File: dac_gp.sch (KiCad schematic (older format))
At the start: 7 parts, among them U10 TMUX6136PWR, U11 TMUX6136PWR, U5 DAC80508ZRTER

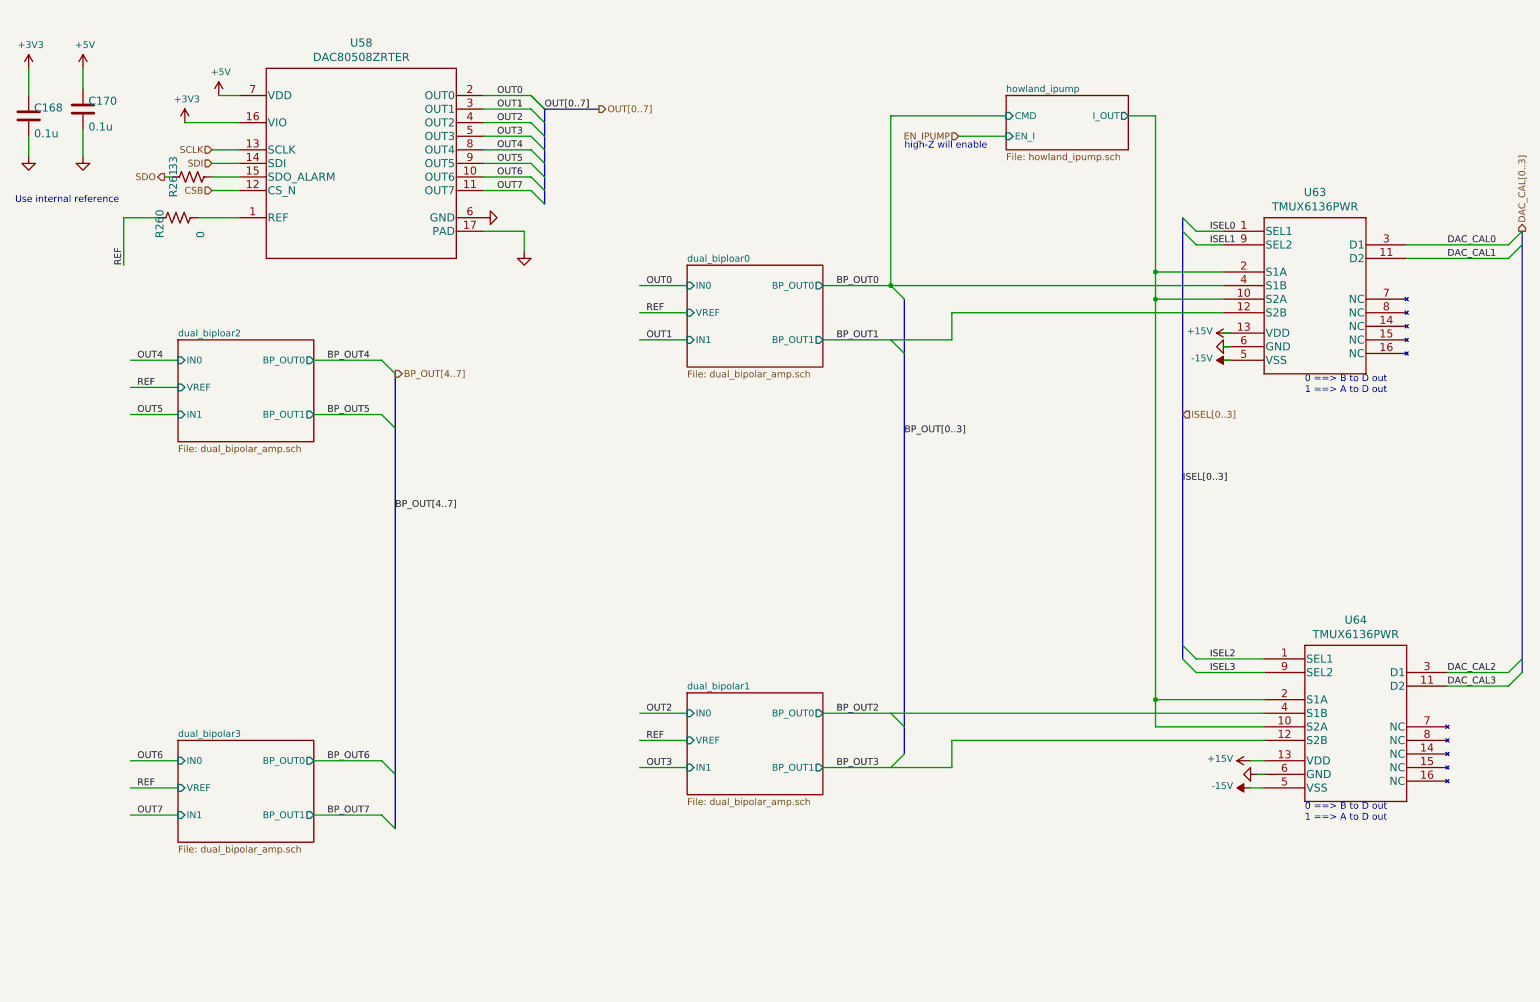
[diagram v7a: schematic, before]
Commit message: reduce ADC and DAC connections to ease routing
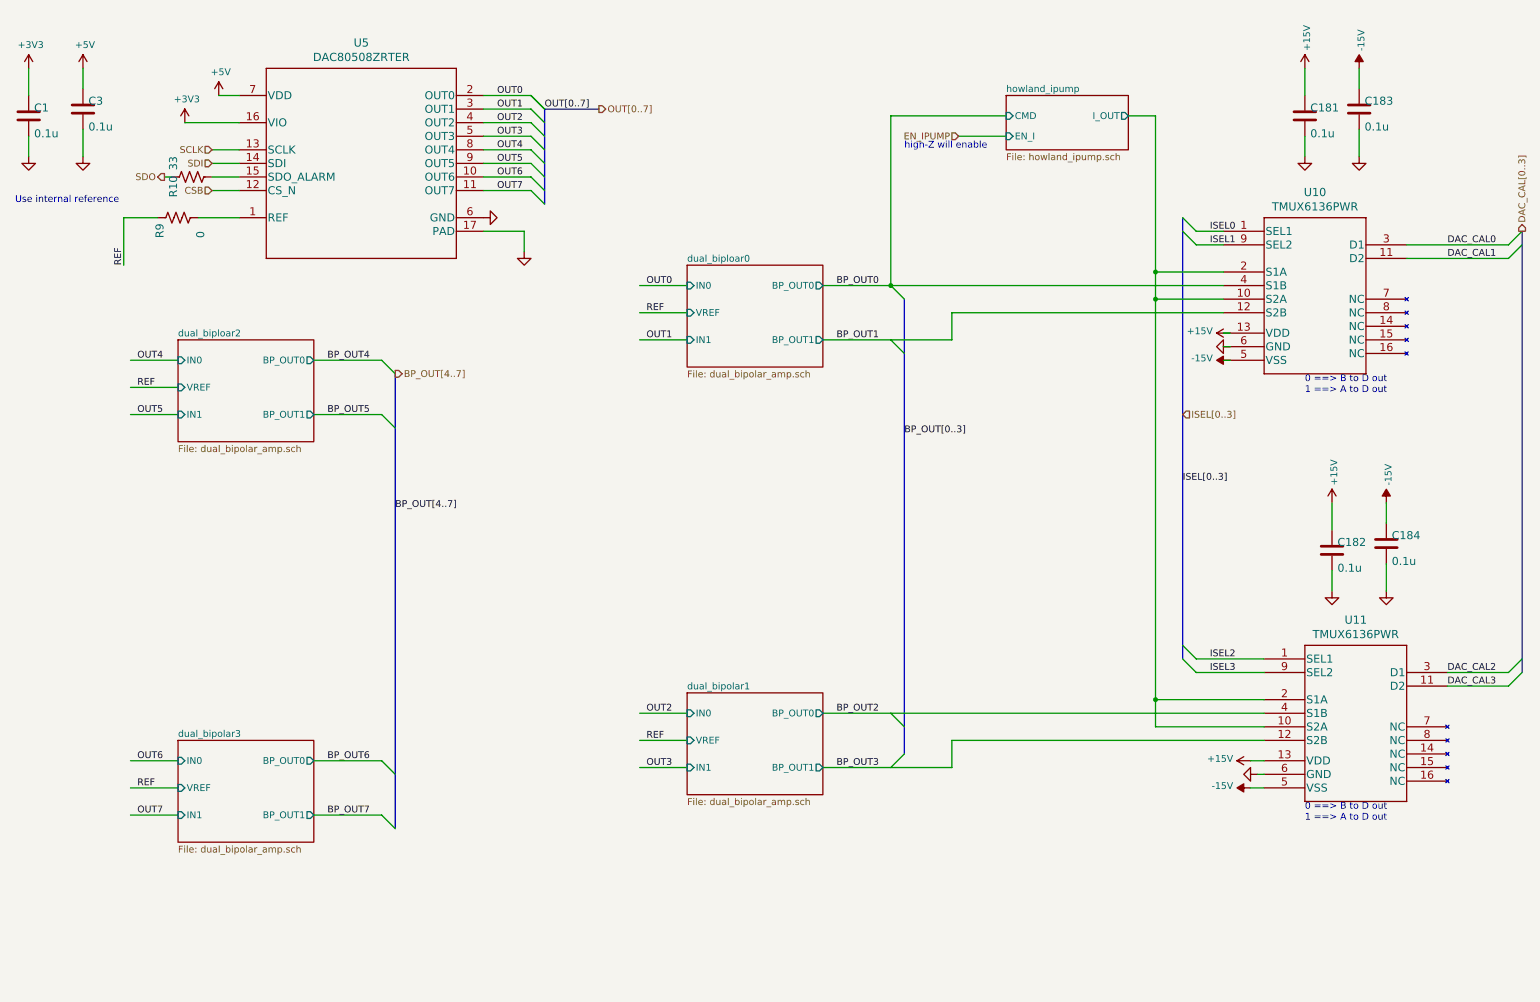
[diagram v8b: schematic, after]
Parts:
- added C181, C182, C183, C184: 0.1u, Capacitor_SMD:C_0603_1608Metric, symbol Device:C
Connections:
- wire segments 75 -> 83
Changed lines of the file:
@@
 $Descr User 12505 8268
 encoding utf-8
-Sheet 21 26
+Sheet 2 26
 Title ""
 Date ""
@@
 AR Path="/6095BD4C/519C2D15" Ref="#FRAME1"  Part="1"
 AR Path="/61B02572/519C2D15" Ref="#FRAME2"  Part="1"
-F 0 "#FRAME2" H 900 6900 50  0001 C CNN
+F 0 "#FRAME1" H 900 6900 50  0001 C CNN
 F 1 "FRAME_A_L" H 900 6900 50  0001 C CNN
 F 2 "" H 900 6900 50  0001 C CNN
@@
 AR Path="/6095BD4C/A7A1DCDA" Ref="C1"  Part="1"
 AR Path="/61B02572/A7A1DCDA" Ref="C168"  Part="1"
-F 0 "C168" H 690 1275 59  0000 L BNN
+F 0 "C1" H 690 1275 59  0000 L BNN
 F 1 "0.1u" H 690 1085 59  0000 L BNN
 F 2 "Capacitor_SMD:C_0603_1608Metric" H 650 1250 50  0001 C CNN
@@
 AR Path="/6095BD4C/46ACB443" Ref="C3"  Part="1"
 AR Path="/61B02572/46ACB443" Ref="C170"  Part="1"
-F 0 "C170" H 1090 1225 59  0000 L BNN
+F 0 "C3" H 1090 1225 59  0000 L BNN
 F 1 "0.1u" H 1090 1035 59  0000 L BNN
 F 2 "Capacitor_SMD:C_0603_1608Metric" H 1050 1200 50  0001 C CNN
@@
 AR Path="/6095BD4C/60A11E5A" Ref="U5"  Part="1"
 AR Path="/61B02572/60A11E5A" Ref="U58"  Part="1"
-F 0 "U58" H 3100 2488 60  0000 C CNN
+F 0 "U5" H 3100 2488 60  0000 C CNN
 F 1 "DAC80508ZRTER" H 3100 2382 60  0000 C CNN
 F 2 "Package_DFN_QFN:WQFN-16-1EP_3x3mm_P0.5mm_EP1.6x1.6mm" H 3100 1540 60  0001 C CNN
@@
 AR Path="/6095BD4C/60A29EE1" Ref="R9"  Part="1"
 AR Path="/61B02572/60A29EE1" Ref="R260"  Part="1"
-F 0 "R260" H 1600 2100 59  0000 L BNN
+F 0 "R9" H 1600 2100 59  0000 L BNN
 F 1 "0" H 1600 1800 59  0000 L BNN
 F 2 "Resistor_SMD:R_0603_1608Metric" H 1750 2000 50  0001 C CNN
@@
 AR Path="/6095BD4C/60B8C0FB" Ref="U10"  Part="1"
 AR Path="/61B02572/60B8C0FB" Ref="U63"  Part="1"
-F 0 "U63" H 10125 2387 60  0000 C CNN
+F 0 "U10" H 10125 2387 60  0000 C CNN
 F 1 "TMUX6136PWR" H 10125 2281 60  0000 C CNN
 F 2 "Package_SO:TSSOP-16_4.4x5mm_P0.65mm" H 10100 2200 60  0001 C CNN
@@
 AR Path="/6095BD4C/60C5A3EA" Ref="U11"  Part="1"
 AR Path="/61B02572/60C5A3EA" Ref="U64"  Part="1"
-F 0 "U64" H 10425 5537 60  0000 C CNN
+F 0 "U11" H 10425 5537 60  0000 C CNN
 F 1 "TMUX6136PWR" H 10425 5431 60  0000 C CNN
 F 2 "Package_SO:TSSOP-16_4.4x5mm_P0.65mm" H 10400 5350 60  0001 C CNN
@@
 AR Path="/6095BD4C/617C87E1" Ref="R10"  Part="1"
 AR Path="/61B02572/617C87E1" Ref="R261"  Part="1"
-F 0 "R261" H 1700 1800 59  0000 L BNN
+F 0 "R10" H 1700 1800 59  0000 L BNN
 F 1 "33" H 1900 1800 59  0000 L BNN
 F 2 "Resistor_SMD:R_0603_1608Metric" H 1850 1700 50  0001 C CNN
@@
 Wire Wire Line
 	2750 6400 3250 6400
+Wire Bus Line
+	7100 2600 7100 5950
+$Comp
+L Device:C C182
+U 1 1 61067784
+P 10250 4450
+AR Path="/6095BD4C/61067784" Ref="C182"  Part="1"
+AR Path="/61B02572/61067784" Ref="C186"  Part="1"
+F 0 "C182" H 10290 4475 59  0000 L BNN
+F 1 "0.1u" H 10290 4285 59  0000 L BNN
+F 2 "Capacitor_SMD:C_0603_1608Metric" H 10250 4450 50  0001 C CNN
+F 3 "" H 10250 4450 50  0001 C CNN
+F 4 "CC0603MRX7R8BB104" H 10250 4450 50  0001 C CNN "Manf#"
+F 5 "Yageo" H 10290 4575 50  0001 C CNN "Manufacturer_Name"
+F 6 "20%" H 10290 4575 50  0001 C CNN "Tolerance"
+F 7 "25" H 10290 4575 50  0001 C CNN "voltage"
+	1    10250 4450
+	1    0    0    -1
+$EndComp
+$Comp
+L Device:C C184
+U 1 1 6106778E
+P 10650 4400
+AR Path="/6095BD4C/6106778E" Ref="C184"  Part="1"
+AR Path="/61B02572/6106778E" Ref="C188"  Part="1"
+F 0 "C184" H 10690 4425 59  0000 L BNN
+F 1 "0.1u" H 10690 4235 59  0000 L BNN
+F 2 "Capacitor_SMD:C_0603_1608Metric" H 10650 4400 50  0001 C CNN
+F 3 "" H 10650 4400 50  0001 C CNN
+F 4 "CC0603MRX7R8BB104" H 10650 4400 50  0001 C CNN "Manf#"
+F 5 "Yageo" H 10690 4525 50  0001 C CNN "Manufacturer_Name"
+F 6 "20%" H 10690 4525 50  0001 C CNN "Tolerance"
+F 7 "25" H 10690 4525 50  0001 C CNN "voltage"
+	1    10650 4400
+	1    0    0    -1
+$EndComp
+$Comp
+L power:GND #GND0282
+U 1 1 61067794
+P 10250 4750
+AR Path="/6095BD4C/61067794" Ref="#GND0282"  Part="1"
+AR Path="/61B02572/61067794" Ref="#GND0286"  Part="1"
+F 0 "#GND0286" H 10250 4750 50  0001 C CNN
+F 1 "GND" H 10150 4650 59  0001 L BNN
+F 2 "" H 10250 4750 50  0001 C CNN
+F 3 "" H 10250 4750 50  0001 C CNN
+	1    10250 4750
+	1    0    0    -1
+$EndComp
+$Comp
+L power:GND #GND0283
+U 1 1 6106779A
+P 10650 4750
+AR Path="/6095BD4C/6106779A" Ref="#GND0283"  Part="1"
+AR Path="/61B02572/6106779A" Ref="#GND0287"  Part="1"
+F 0 "#GND0287" H 10650 4750 50  0001 C CNN
+F 1 "GND" H 10550 4650 59  0001 L BNN
+F 2 "" H 10650 4750 50  0001 C CNN
+F 3 "" H 10650 4750 50  0001 C CNN
+	1    10650 4750
+	1    0    0    -1
+$EndComp
+Wire Wire Line
+	10650 4100 10650 4250
+Wire Wire Line
+	10650 4550 10650 4750
+Wire Wire Line
+	10250 4100 10250 4300
+Wire Wire Line
+	10250 4750 10250 4600
+$Comp
+L Device:C C181
+U 1 1 6106B5C5
+P 10050 1250
+AR Path="/6095BD4C/6106B5C5" Ref="C181"  Part="1"
+AR Path="/61B02572/6106B5C5" Ref="C185"  Part="1"
+F 0 "C181" H 10090 1275 59  0000 L BNN
+F 1 "0.1u" H 10090 1085 59  0000 L BNN
+F 2 "Capacitor_SMD:C_0603_1608Metric" H 10050 1250 50  0001 C CNN
+F 3 "" H 10050 1250 50  0001 C CNN
+F 4 "CC0603MRX7R8BB104" H 10050 1250 50  0001 C CNN "Manf#"
+F 5 "Yageo" H 10090 1375 50  0001 C CNN "Manufacturer_Name"
+F 6 "20%" H 10090 1375 50  0001 C CNN "Tolerance"
+F 7 "25" H 10090 1375 50  0001 C CNN "voltage"
+	1    10050 1250
+	1    0    0    -1
+$EndComp
+$Comp
+L Device:C C183
+U 1 1 6106B5CF
+P 10450 1200
+AR Path="/6095BD4C/6106B5CF" Ref="C183"  Part="1"
+AR Path="/61B02572/6106B5CF" Ref="C187"  Part="1"
+F 0 "C183" H 10490 1225 59  0000 L BNN
+F 1 "0.1u" H 10490 1035 59  0000 L BNN
+F 2 "Capacitor_SMD:C_0603_1608Metric" H 10450 1200 50  0001 C CNN
+F 3 "" H 10450 1200 50  0001 C CNN
+F 4 "CC0603MRX7R8BB104" H 10450 1200 50  0001 C CNN "Manf#"
+F 5 "Yageo" H 10490 1325 50  0001 C CNN "Manufacturer_Name"
+F 6 "20%" H 10490 1325 50  0001 C CNN "Tolerance"
+F 7 "25" H 10490 1325 50  0001 C CNN "voltage"
+	1    10450 1200
+	1    0    0    -1
+$EndComp
+$Comp
+L power:GND #GND0284
+U 1 1 6106B5D5
+P 10050 1550
+AR Path="/6095BD4C/6106B5D5" Ref="#GND0284"  Part="1"
+AR Path="/61B02572/6106B5D5" Ref="#GND0288"  Part="1"
+F 0 "#GND0288" H 10050 1550 50  0001 C CNN
+F 1 "GND" H 9950 1450 59  0001 L BNN
+F 2 "" H 10050 1550 50  0001 C CNN
+F 3 "" H 10050 1550 50  0001 C CNN
+	1    10050 1550
+	1    0    0    -1
+$EndComp
+$Comp
+L power:GND #GND0285
+U 1 1 6106B5DB
+P 10450 1550
+AR Path="/6095BD4C/6106B5DB" Ref="#GND0285"  Part="1"
+AR Path="/61B02572/6106B5DB" Ref="#GND0289"  Part="1"
+F 0 "#GND0289" H 10450 1550 50  0001 C CNN
+F 1 "GND" H 10350 1450 59  0001 L BNN
+F 2 "" H 10450 1550 50  0001 C CNN
+F 3 "" H 10450 1550 50  0001 C CNN
+	1    10450 1550
+	1    0    0    -1
+$EndComp
+Wire Wire Line
+	10450 900  10450 1050
+Wire Wire Line
+	10450 1350 10450 1550
+Wire Wire Line
+	10050 900  10050 1100
+Wire Wire Line
+	10050 1550 10050 1400
 Wire Wire Line
 	6500 5650 9750 5650
@@
 	3350 3150 3350 6500
 Wire Bus Line
-	7100 2600 7100 5950
-Wire Bus Line
 	4450 1200 4450 1900
+$Comp
+L power:-15V #PWR0277
+U 1 1 6106DFBA
+P 10650 4100
+AR Path="/6095BD4C/6106DFBA" Ref="#PWR0277"  Part="1"
+AR Path="/61B02572/6106DFBA" Ref="#PWR0281"  Part="1"
+F 0 "#PWR0281" H 10650 4200 50  0001 C CNN
+F 1 "-15V" V 10665 4228 50  0000 L CNN
+F 2 "" H 10650 4100 50  0001 C CNN
+F 3 "" H 10650 4100 50  0001 C CNN
+	1    10650 4100
+	1    0    0    -1
+$EndComp
+$Comp
+L power:+15V #PWR0278
+U 1 1 6106E58F
+P 10250 4100
+AR Path="/6095BD4C/6106E58F" Ref="#PWR0278"  Part="1"
+AR Path="/61B02572/6106E58F" Ref="#PWR0282"  Part="1"
+F 0 "#PWR0282" H 10250 3950 50  0001 C CNN
+F 1 "+15V" V 10265 4228 50  0000 L CNN
+F 2 "" H 10250 4100 50  0001 C CNN
+F 3 "" H 10250 4100 50  0001 C CNN
+	1    10250 4100
+	1    0    0    -1
+$EndComp
+$Comp
+L power:+15V #PWR0279
+U 1 1 6106ECCF
+P 10050 900
+AR Path="/6095BD4C/6106ECCF" Ref="#PWR0279"  Part="1"
+AR Path="/61B02572/6106ECCF" Ref="#PWR0283"  Part="1"
+F 0 "#PWR0283" H 10050 750 50  0001 C CNN
+F 1 "+15V" V 10065 1028 50  0000 L CNN
+F 2 "" H 10050 900 50  0001 C CNN
+F 3 "" H 10050 900 50  0001 C CNN
+	1    10050 900
+	1    0    0    -1
+$EndComp
+$Comp
+L power:-15V #PWR0280
+U 1 1 6106F147
+P 10450 900
+AR Path="/6095BD4C/6106F147" Ref="#PWR0280"  Part="1"
+AR Path="/61B02572/6106F147" Ref="#PWR0284"  Part="1"
+F 0 "#PWR0284" H 10450 1000 50  0001 C CNN
+F 1 "-15V" V 10465 1028 50  0000 L CNN
+F 2 "" H 10450 900 50  0001 C CNN
+F 3 "" H 10450 900 50  0001 C CNN
+	1    10450 900
+	1    0    0    -1
+$EndComp
 $EndSCHEMATC
